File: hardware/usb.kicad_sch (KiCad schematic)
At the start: 3 parts, among them J6 USB_C_Receptacle, J7 USB_C_Receptacle, J8 USB_C_Receptacle

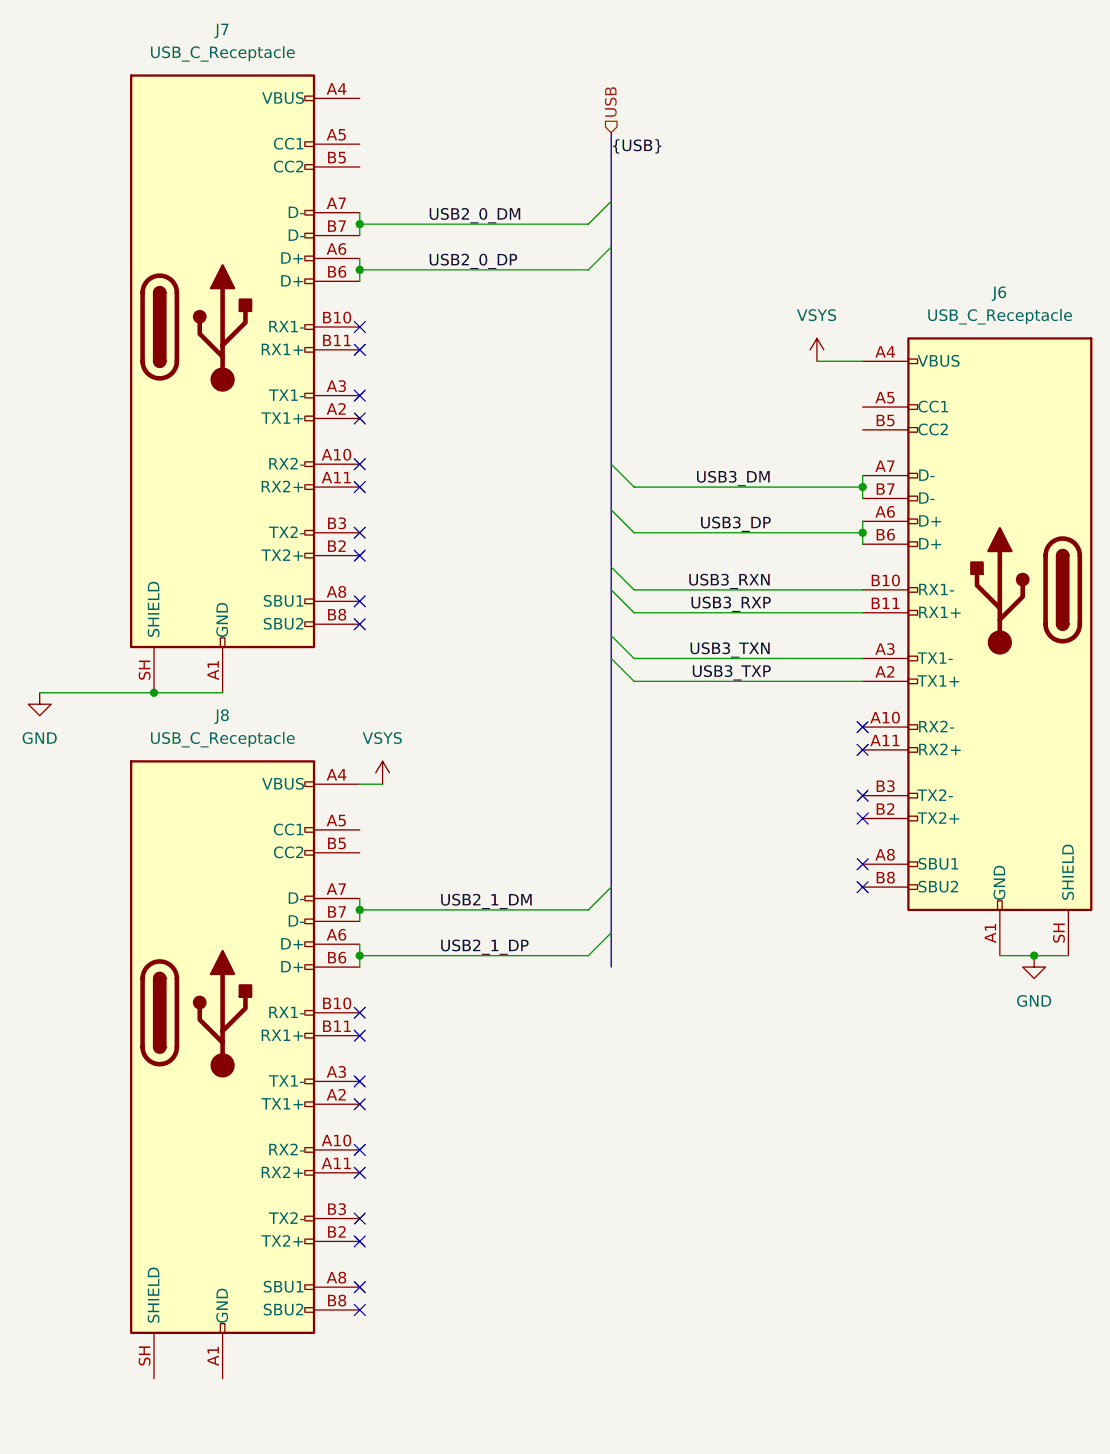
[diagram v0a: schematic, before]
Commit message: component Placement
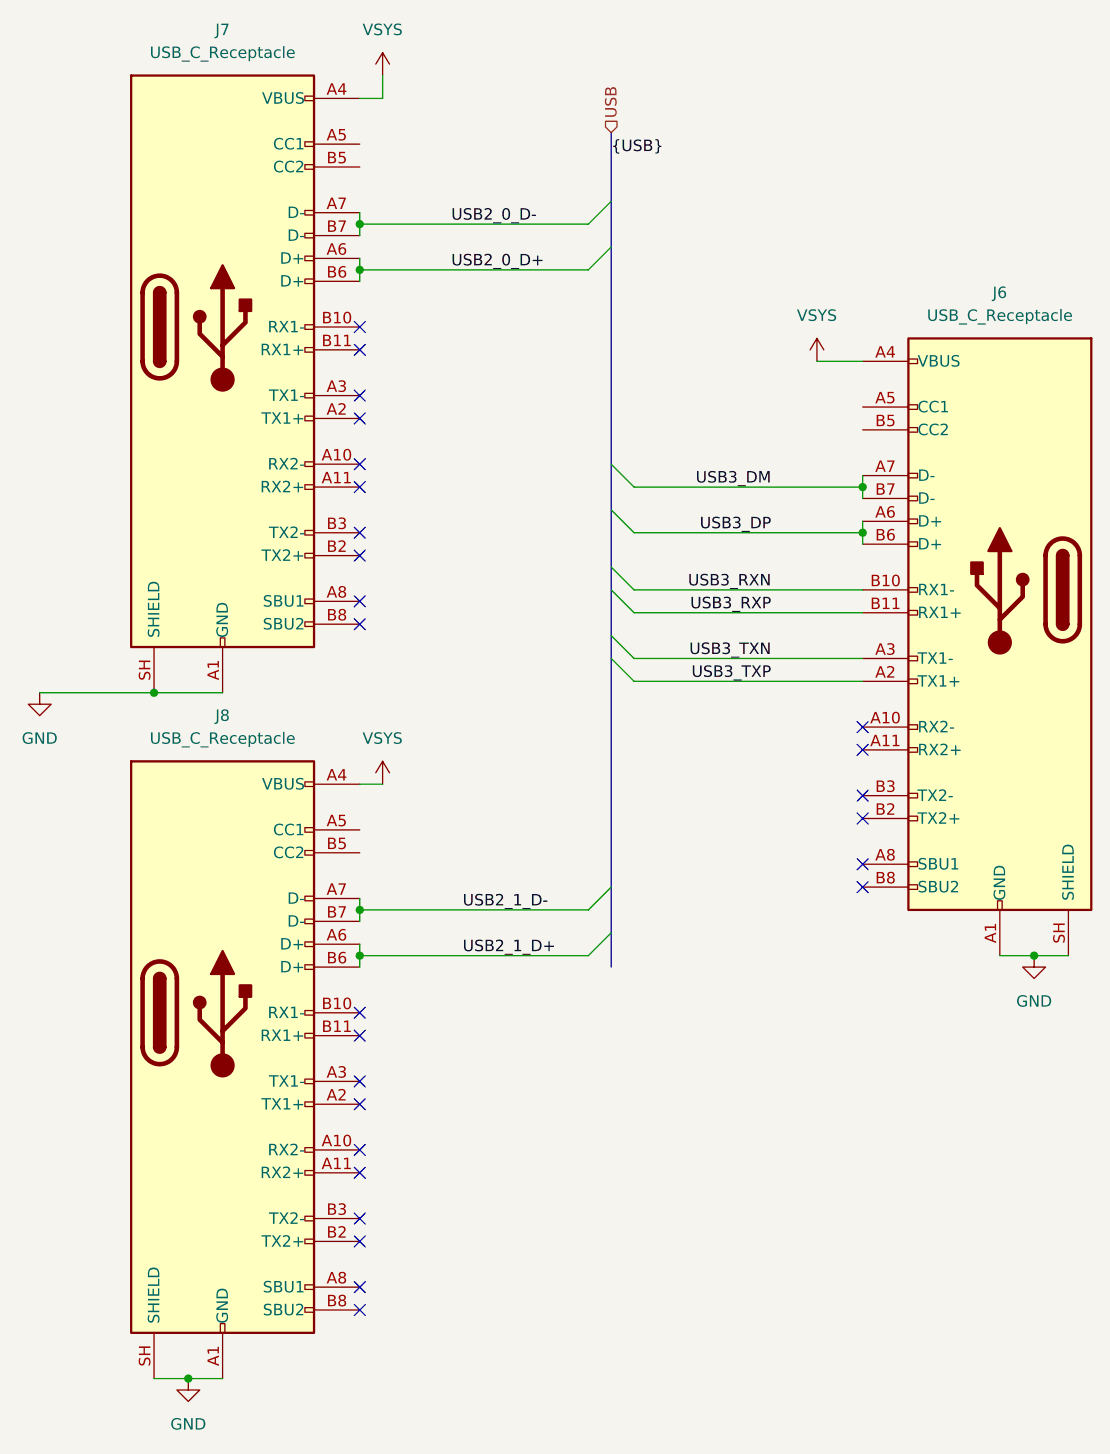
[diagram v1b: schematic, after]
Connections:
- net GND: now also J8.A1 (GND), J8.A12 (GND), J8.B1 (GND), J8.B12 (GND), J8.SH (SHIELD)
- net VSYS: now also J7.A4 (VBUS), J7.A9 (VBUS), J7.B4 (VBUS), J7.B9 (VBUS)
- net USB2_0_DM renamed USB2_0_D-
- net USB2_0_DP renamed USB2_0_D+
- net USB2_1_DM renamed USB2_1_D-
- net USB2_1_DP renamed USB2_1_D+
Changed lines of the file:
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@@
+	)
+	(junction
+		(at 74.93 175.26)
+		(diameter 0)
+		(color 0 0 0 0)
 	)
 	(junction
@@
 	(wire
 		(pts
+			(xy 96.52 33.02) (xy 93.98 33.02)
+		)
+		(stroke
+			(width 0)
+			(type default)
+		)
+	)
+	(wire
+		(pts
 			(xy 149.86 62.23) (xy 144.78 62.23)
 		)
@@
 	(wire
 		(pts
+			(xy 74.93 175.26) (xy 78.74 175.26)
+		)
+		(stroke
+			(width 0)
+			(type default)
+		)
+	)
+	(wire
+		(pts
 			(xy 93.98 46.99) (xy 93.98 48.26)
 		)
@@
 	(wire
 		(pts
+			(xy 71.12 175.26) (xy 74.93 175.26)
+		)
+		(stroke
+			(width 0)
+			(type default)
+		)
+	)
+	(wire
+		(pts
 			(xy 93.98 123.19) (xy 119.38 123.19)
+		)
+		(stroke
+			(width 0)
+			(type default)
+		)
+	)
+	(wire
+		(pts
+			(xy 96.52 30.48) (xy 96.52 33.02)
 		)
 		(stroke
@@
 		)
 	)
-	(label "USB2_1_DP"
-		(at 102.87 128.27 0)
-		(effects
-			(font
-				(size 1.27 1.27)
-			)
-			(justify left bottom)
-		)
-	)
 	(label "USB3_TXP"
 		(at 139.7 97.79 180)
@@
 		)
 	)
-	(label "USB2_0_DP"
-		(at 101.6 52.07 0)
-		(effects
-			(font
-				(size 1.27 1.27)
-			)
-			(justify left bottom)
-		)
-	)
 	(label "USB3_TXN"
 		(at 139.7 95.25 180)
@@
 		)
 	)
-	(label "USB2_0_DM"
-		(at 101.6 46.99 0)
+	(label "USB2_1_D+"
+		(at 105.41 128.27 0)
+		(effects
+			(font
+				(size 1.27 1.27)
+			)
+			(justify left bottom)
+		)
+	)
+	(label "USB2_1_D-"
+		(at 105.41 123.19 0)
 		(effects
 			(font
@@
 		)
 	)
-	(label "USB2_1_DM"
-		(at 102.87 123.19 0)
+	(label "USB2_0_D+"
+		(at 104.14 52.07 0)
 		(effects
 			(font
@@
 			)
 			(justify right bottom)
+		)
+	)
+	(label "USB2_0_D-"
+		(at 104.14 46.99 0)
+		(effects
+			(font
+				(size 1.27 1.27)
+			)
+			(justify left bottom)
 		)
 	)
@@
 	)
 	(symbol
+		(lib_id "power:GND")
+		(at 74.93 175.26 0)
+		(mirror y)
+		(unit 1)
+		(body_style 1)
+		(exclude_from_sim no)
+		(in_bom yes)
+		(on_board yes)
+		(in_pos_files yes)
+		(dnp no)
+		(fields_autoplaced yes)
+		(property "Reference" "#PWR072"
+			(at 74.93 181.61 0)
+			(hide yes)
+			(show_name no)
+			(do_not_autoplace no)
+			(effects
+				(font
+					(size 1.27 1.27)
+				)
+			)
+		)
+		(property "Value" "GND"
+			(at 74.93 180.34 0)
+			(show_name no)
+			(do_not_autoplace no)
+			(effects
+				(font
+					(size 1.27 1.27)
+				)
+			)
+		)
+		(property "Footprint" ""
+			(at 74.93 175.26 0)
+			(hide yes)
+			(show_name no)
+			(do_not_autoplace no)
+			(effects
+				(font
+					(size 1.27 1.27)
+				)
+			)
+		)
+		(property "Datasheet" ""
+			(at 74.93 175.26 0)
+			(hide yes)
+			(show_name no)
+			(do_not_autoplace no)
+			(effects
+				(font
+					(size 1.27 1.27)
+				)
+			)
+		)
+		(property "Description" "Power symbol creates a global label with name \"GND\" , ground"
+			(at 74.93 175.26 0)
+			(hide yes)
+			(show_name no)
+			(do_not_autoplace no)
+			(effects
+				(font
+					(size 1.27 1.27)
+				)
+			)
+		)
+		(pin "1"
+		)
+		(instances
+			(project "mini-server"
+				(path "/17ecef2a-4000-49de-93ef-dcbfcfdaa69f/a6b568fb-a2c2-40e2-8f9e-cce7ed64309a"
+					(reference "#PWR072")
+					(unit 1)
+				)
+			)
+		)
+	)
+	(symbol
 		(lib_id "Connector:USB_C_Receptacle")
 		(at 165.1 87.63 0)
@@
 					(unit 1)
 				)
+			)
+		)
+	)
+	(symbol
+		(lib_id "power:VBUS")
+		(at 96.52 30.48 0)
+		(mirror y)
+		(unit 1)
+		(body_style 1)
+		(exclude_from_sim no)
+		(in_bom yes)
+		(on_board yes)
+		(in_pos_files yes)
+		(dnp no)
+		(fields_autoplaced yes)
+		(property "Reference" "#PWR073"
+			(at 96.52 34.29 0)
+			(hide yes)
+			(show_name no)
+			(do_not_autoplace no)
+			(effects
+				(font
+					(size 1.27 1.27)
+				)
+			)
+		)
+		(property "Value" "VSYS"
+			(at 96.52 25.4 0)
+			(show_name no)
+			(do_not_autoplace no)
+			(effects
+				(font
+					(size 1.27 1.27)
+				)
+			)
+		)
+		(property "Footprint" ""
+			(at 96.52 30.48 0)
+			(hide yes)
+			(show_name no)
+			(do_not_autoplace no)
+			(effects
+				(font
+					(size 1.27 1.27)
+				)
+			)
+		)
+		(property "Datasheet" ""
+			(at 96.52 30.48 0)
+			(hide yes)
+			(show_name no)
+			(do_not_autoplace no)
+			(effects
+				(font
+					(size 1.27 1.27)
+				)
+			)
+		)
+		(property "Description" "Power symbol creates a global label with name \"VBUS\""
+			(at 96.52 30.48 0)
+			(hide yes)
+			(show_name no)
+			(do_not_autoplace no)
+			(effects
+				(font
+					(size 1.27 1.27)
+				)
+			)
+		)
+		(pin "1"
+		)
+		(instances
+			(project "mini-server"
+				(path "/17ecef2a-4000-49de-93ef-dcbfcfdaa69f/a6b568fb-a2c2-40e2-8f9e-cce7ed64309a"
+					(reference "#PWR073")
+					(unit 1)
+				)

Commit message: routing
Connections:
- net USB3_DM renamed USB3_D-
- net USB3_DP renamed USB3_D+
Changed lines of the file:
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@@
 		)
 	)
-	(label "USB3_DP"
+	(label "USB3_D+"
 		(at 139.7 81.28 180)
 		(effects
@@
 		)
 	)
-	(label "USB3_DM"
+	(label "USB3_D-"
 		(at 139.7 76.2 180)
 		(effects

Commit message: touch up on lots of small things
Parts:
- added C74, C75: 100n, Capacitor_SMD:C_0201_0603Metric, symbol Device:C_Small
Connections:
- net USB3_TXN: now also C74.1; no longer J6.A3 (TX1-)
- net USB3_TXP: now also C75.1; no longer J6.A2 (TX1+)
- new net: C75.2, J6.A2 (TX1+)
- new net: C74.2, J6.A3 (TX1-)
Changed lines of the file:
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@@
+	(wire
+		(pts
+			(xy 143.51 95.25) (xy 149.86 95.25)
+		)
+		(stroke
+			(width 0)
+			(type default)
+		)
+	)
+	(wire
+		(pts
+			(xy 148.59 97.79) (xy 149.86 97.79)
+		)
+		(stroke
+			(width 0)
+			(type default)
+		)
+	)
 	(wire
 		(pts
@@
 	(wire
 		(pts
-			(xy 149.86 97.79) (xy 124.46 97.79)
-		)
-		(stroke
-			(width 0)
-			(type default)
-		)
-	)
-	(wire
-		(pts
 			(xy 93.98 52.07) (xy 93.98 53.34)
 		)
@@
 	(wire
 		(pts
+			(xy 124.46 97.79) (xy 143.51 97.79)
+		)
+		(stroke
+			(width 0)
+			(type default)
+		)
+	)
+	(wire
+		(pts
 			(xy 74.93 175.26) (xy 78.74 175.26)
 		)
@@
 	(wire
 		(pts
-			(xy 149.86 95.25) (xy 124.46 95.25)
-		)
-		(stroke
-			(width 0)
-			(type default)
-		)
-	)
-	(wire
-		(pts
 			(xy 93.98 52.07) (xy 119.38 52.07)
+		)
+		(stroke
+			(width 0)
+			(type default)
+		)
+	)
+	(wire
+		(pts
+			(xy 124.46 95.25) (xy 138.43 95.25)
 		)
 		(stroke
@@
 	)
 	(label "USB3_TXP"
-		(at 139.7 97.79 180)
-		(effects
-			(font
-				(size 1.27 1.27)
-			)
-			(justify right bottom)
+		(at 127 97.79 0)
+		(effects
+			(font
+				(size 1.27 1.27)
+			)
+			(justify left bottom)
 		)
 	)
 	(label "USB3_TXN"
-		(at 139.7 95.25 180)
-		(effects
-			(font
-				(size 1.27 1.27)
-			)
-			(justify right bottom)
+		(at 127 95.25 0)
+		(effects
+			(font
+				(size 1.27 1.27)
+			)
+			(justify left bottom)
 		)
 	)
@@
 		)
 	)
+	(symbol
+		(lib_id "Device:C_Small")
+		(at 146.05 97.79 90)
+		(unit 1)
+		(body_style 1)
+		(exclude_from_sim no)
+		(in_bom yes)
+		(on_board yes)
+		(in_pos_files yes)
+		(dnp no)
+		(property "Reference" "C75"
+			(at 141.478 99.314 90)
+			(show_name no)
+			(do_not_autoplace no)
+			(effects
+				(font
+					(size 1.27 1.27)
+				)
+				(justify right)
+			)
+		)
+		(property "Value" "100n"
+			(at 140.97 101.092 90)
+			(show_name no)
+			(do_not_autoplace no)
+			(effects
+				(font
+					(size 1.27 1.27)
+				)
+				(justify right)
+			)
+		)
+		(property "Footprint" "Capacitor_SMD:C_0201_0603Metric"
+			(at 146.05 97.79 0)
+			(hide yes)
+			(show_name no)
+			(do_not_autoplace no)
+			(effects
+				(font
+					(size 1.27 1.27)
+				)
+			)
+		)
+		(property "Datasheet" ""
+			(at 146.05 97.79 0)
+			(hide yes)
+			(show_name no)
+			(do_not_autoplace no)
+			(effects
+				(font
+					(size 1.27 1.27)
+				)
+			)
+		)
+		(property "Description" "Unpolarized capacitor, small symbol"
+			(at 146.05 97.79 0)
+			(hide yes)
+			(show_name no)
+			(do_not_autoplace no)
+			(effects
+				(font
+					(size 1.27 1.27)
+				)
+			)
+		)
+		(pin "1"
+		)
+		(pin "2"
+		)
+		(instances
+			(project "mini-server"
+				(path "/17ecef2a-4000-49de-93ef-dcbfcfdaa69f/a6b568fb-a2c2-40e2-8f9e-cce7ed64309a"
+					(reference "C75")
+					(unit 1)
+				)
+			)
+		)
+	)
+	(symbol
+		(lib_id "Device:C_Small")
+		(at 140.97 95.25 90)
+		(unit 1)
+		(body_style 1)
+		(exclude_from_sim no)
+		(in_bom yes)
+		(on_board yes)
+		(in_pos_files yes)
+		(dnp no)
+		(property "Reference" "C74"
+			(at 142.494 92.202 90)
+			(show_name no)
+			(do_not_autoplace no)
+			(effects
+				(font
+					(size 1.27 1.27)
+				)
+				(justify right)
+			)
+		)
+		(property "Value" "100n"
+			(at 141.986 93.98 90)
+			(show_name no)
+			(do_not_autoplace no)
+			(effects
+				(font
+					(size 1.27 1.27)
+				)
+				(justify right)
+			)
+		)
+		(property "Footprint" "Capacitor_SMD:C_0201_0603Metric"
+			(at 140.97 95.25 0)
+			(hide yes)
+			(show_name no)
+			(do_not_autoplace no)
+			(effects
+				(font
+					(size 1.27 1.27)
+				)
+			)
+		)
+		(property "Datasheet" ""
+			(at 140.97 95.25 0)
+			(hide yes)
+			(show_name no)
+			(do_not_autoplace no)
+			(effects
+				(font
+					(size 1.27 1.27)
+				)
+			)
+		)
+		(property "Description" "Unpolarized capacitor, small symbol"
+			(at 140.97 95.25 0)
+			(hide yes)
+			(show_name no)
+			(do_not_autoplace no)
+			(effects
+				(font
+					(size 1.27 1.27)
+				)
+			)
+		)
+		(pin "1"
+		)
+		(pin "2"
+		)
+		(instances
+			(project "mini-server"
+				(path "/17ecef2a-4000-49de-93ef-dcbfcfdaa69f/a6b568fb-a2c2-40e2-8f9e-cce7ed64309a"
+					(reference "C74")
+					(unit 1)
+				)
+			)
+		)
+	)
